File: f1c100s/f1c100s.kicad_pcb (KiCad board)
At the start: 2 copper layers, 47.6 x 52.6 mm, 74 parts, among them IC1 F1C100S, IC2 MCP1703T-2802E_CB, IC3 MCP1703T-2802E_CB, IC4 MCP1703T-2802E_CB, IC5 MCP1703T-2802E_CB, IC6 S25FL256SAGNFI001, J1 USB_B_Micro, J2 Conn_02x18_Odd_Even, J3 Conn_01x06, J4 Conn_02x02_Odd_Even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

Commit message: Work in progress...
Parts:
- added REF**: MountingHole_2.2mm_M2, MountingHole:MountingHole_2.2mm_M2, F.Cu at (190.9, 97.6)
- added REF**: MountingHole_2.2mm_M2, MountingHole:MountingHole_2.2mm_M2, F.Cu at (149.4, 97.7)
- added REF**: MountingHole_2.2mm_M2, MountingHole:MountingHole_2.2mm_M2, F.Cu at (149.4, 52.9)
- added REF**: MountingHole_2.2mm_M2, MountingHole:MountingHole_2.2mm_M2, F.Cu at (190.9, 52.9)
- moved D1 9.40 mm to (160.0, 96.0)
- moved R10 9.40 mm to (163.5, 99.9)
- moved R8 9.40 mm to (163.5, 96.7)
- moved R9 9.40 mm to (163.5, 98.3)
- moved TP1 6.64 mm to (184.4, 99.1)
- moved C18 5.49 mm to (166.5, 52.4)
- moved C19 5.49 mm to (170.1, 54.3)
- moved C21 5.49 mm to (170.7, 55.9)
- moved C23 5.49 mm to (171.3, 54.3)
- moved C35 5.49 mm to (174.7, 52.7)
- moved C36 5.49 mm to (178.8, 52.7)
- moved C37 5.49 mm to (183.2, 52.7)
- moved R3 5.49 mm to (174.7, 54.8)
- moved C17 5.49 mm to (174.7, 53.7)
- moved R4 5.49 mm to (166.5, 53.4)
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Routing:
- net +3V3: track 102.7 -> 235.1 mm, vias 6 -> 16
- net +5V: track 61.0 -> 147.4 mm, vias 1 -> 4
- net GND: track 0.00 -> 72.0 mm, vias 0 -> 16
- net LCD_D20: track 0.00 -> 59.9 mm, vias 0 -> 2
- net LCD_D19: track 0.00 -> 57.9 mm, vias 0 -> 2
- net LCD_D18: track 0.00 -> 49.6 mm, vias 0 -> 2
- net +1V2: track 19.8 -> 66.9 mm, vias 1 -> 4
- net +2V8: track 32.6 -> 78.5 mm, vias 3 -> 5
- net LCD_D15: track 0.00 -> 44.7 mm, vias 0 -> 1
- net LCD_D3: track 0.00 -> 43.3 mm, vias 0 -> 1
- net SPI0_CLK: track 46.3 -> 3.19 mm, vias 3 -> 1
- net LCD_D14: track 0.00 -> 43.1 mm, vias 0 -> 1
- net LCD_D13: track 0.00 -> 41.7 mm, vias 0 -> 1
- net LCD_D4: track 0.00 -> 41.6 mm, vias 0 -> 1
- net LCD_D12: track 0.00 -> 41.4 mm, vias 0 -> 1
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- added copper zone on In2.Cu, net GND
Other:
- board size 47.6 x 52.6 mm -> 47.6 x 57.7 mm
- copper layers 2 -> 4
- net class Default: clearance 0.2 -> 0.09
- rule trace_clearance: 0.2 -> 0.09
- rule trace_min: 0.127 -> 0.09
- rule via_min_drill: 0.3 -> 0.2
- rule via_min_size: 0.6 -> 0.45

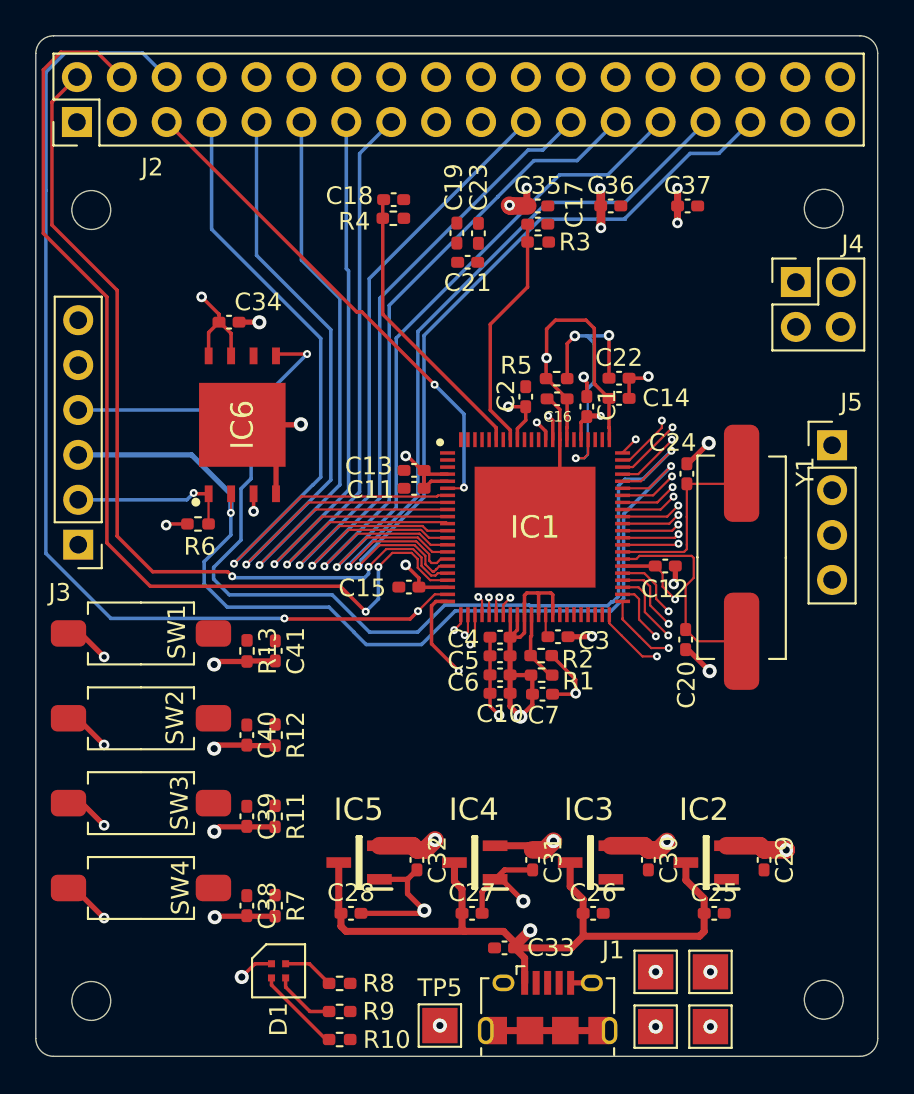
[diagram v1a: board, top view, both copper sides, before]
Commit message: Sadly I have to use a little bit more of GND
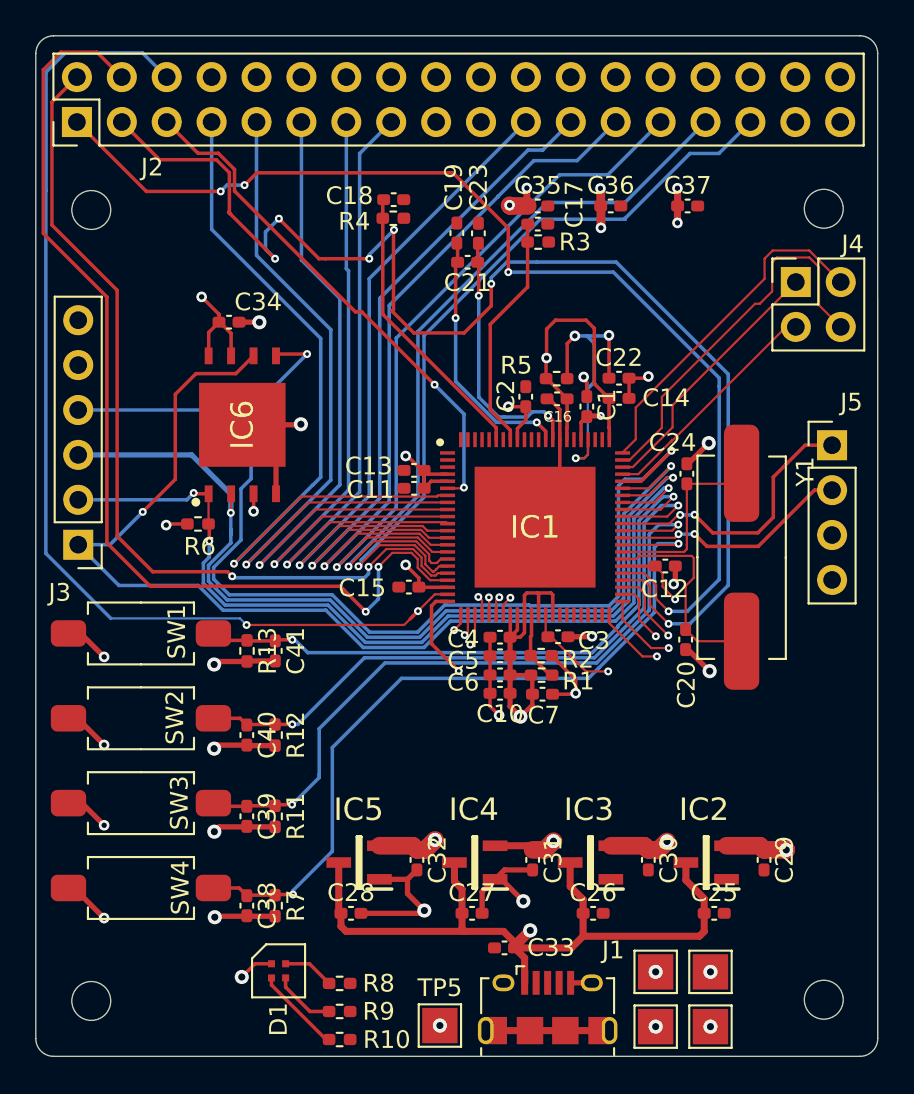
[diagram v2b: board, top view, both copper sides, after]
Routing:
- net LCD_D1: track 4.25 -> 74.3 mm, vias 1 -> 6
- net LCD_D0: track 3.96 -> 63.6 mm, vias 1 -> 4
- net SPI0_CLK: track 3.19 -> 62.5 mm, vias 1 -> 2
- net DEBUG_SW4: track 3.19 -> 43.7 mm, vias 1 -> 2
- net SPI0_CS: track 12.5 -> 50.7 mm, vias 2 -> 3
- net DEBUG_SW3: track 3.30 -> 40.4 mm, vias 1 -> 2
- net DEBUG_SW2: track 3.41 -> 37.8 mm, vias 1 -> 2
- net DEBUG_SW1: track 3.18 -> 36.2 mm, vias 1 -> 2
- net TPX2: track 3.39 -> 22.0 mm, vias 1 -> 0
- net TPX1: track 1.08 -> 19.6 mm, vias 1 -> 0
- net /MPU/TV_VRP: track 1.19 -> 14.6 mm, vias 1 -> 2
- net /MPU/TV_VRN: track 1.46 -> 14.8 mm, vias 1 -> 2
- net UART0_RX: track 3.36 -> 15.9 mm, vias 1 -> 2
- net TPY1: track 3.76 -> 14.9 mm, vias 1 -> 0
- net UART0_TX: track 3.25 -> 13.5 mm, vias 1 -> 2
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
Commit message: Almost ready
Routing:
- net LCD_D21: track 1.03 -> 65.1 mm
- net LCD_D22: track 1.23 -> 64.5 mm
- net LCD_D23: track 1.80 -> 63.9 mm
- net LCD_D16: track 4.30 -> 51.2 mm
- net LCD_D8: track 4.33 -> 51.2 mm, vias 1 -> 4
- net LCD_D17: track 4.33 -> 50.0 mm
- net LCD_DE: track 0.98 -> 45.9 mm, vias 1 -> 2
- net LCD_VSYNC: track 1.12 -> 44.7 mm, vias 1 -> 3
- net DEBUG_LED3: track 0.00 -> 43.2 mm, vias 0 -> 2
- net LCD_HSYNC: track 1.06 -> 43.8 mm, vias 1 -> 3
- net DEBUG_LED2: track 0.00 -> 40.6 mm, vias 0 -> 2
- net LCD_CLK: track 1.09 -> 41.2 mm, vias 1 -> 5
- net LCD_D9: track 3.54 -> 43.3 mm, vias 1 -> 2
- net DEBUG_LED1: track 0.00 -> 38.7 mm, vias 0 -> 2
- net DEBUG_SW1: track 36.2 -> 53.1 mm
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
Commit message: All done i guess. DRC a little bit fuzzy but whatever.
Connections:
- net USB_DM renamed USB_N
- net USB_DP renamed USB_P
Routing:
- net GND: track 71.8 -> 113.4 mm, vias 16 -> 36
- net USB_N: track 1.02 -> 36.4 mm, vias 1 -> 2
- net USB_P: track 1.13 -> 35.3 mm, vias 1 -> 2
- net LCD_VSYNC: track 44.7 -> 48.7 mm
- net LCD_HSYNC: track 43.8 -> 47.5 mm
- net LCD_DE: track 45.9 -> 49.2 mm
- net +5V: track 147.4 -> 146.4 mm
- net DEBUG_SW4: track 46.0 -> 46.8 mm

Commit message: Production files generated.
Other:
- board text added: "F1C100s Linux Dev Board"
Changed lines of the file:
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@@
   (general
     (thickness 1.6)
-    (drawings 8)
+    (drawings 9)
     (tracks 1324)
     (zones 0)
@@
       (outputformat 1)
       (mirror false)
-      (drillshape 1)
+      (drillshape 0)
       (scaleselection 1)
-      (outputdirectory ""))
+      (outputdirectory "../Output/"))
   )
   (net 0 "")
@@
     (tags "Integrated Circuit")
     (attr smd)
-    (fp_text reference IC6 (at 0 0 90) (layer F.SilkS)
+    (fp_text reference IC6 (at 1.6502 4.0874 180) (layer F.SilkS)
       (effects (font (size 1.27 1.27) (thickness 0.254)))
     )
@@
     (at 160.01238 95.98914 270)
     (attr smd)
-    (fp_text reference D1 (at 2.7432 0 270) (layer F.SilkS)
+    (fp_text reference D1 (at 2.3749 0.77978) (layer F.SilkS)
       (effects (font (size 1 1) (thickness 0.15)))
     )
@@
   (module f1c100s:LFXTAL036533 (layer F.Cu)
     (at 186.2074 72.5932 90)
-    (fp_text reference Y1 (at 4.85 3.6 90) (layer F.SilkS)
+    (fp_text reference Y1 (at 0.0432 0.1426 90) (layer F.SilkS)
       (effects (font (size 1 1) (thickness 0.15)))
     )
@@
     (tags "capacitor handsolder")
     (attr smd)
-    (fp_text reference C2 (at 0.05588 -1.1176 90) (layer F.SilkS)
+    (fp_text reference C2 (at -0.28984 -0.99508 90) (layer F.SilkS)
       (effects (font (size 1 1) (thickness 0.15)))
     )
@@
     (tags "capacitor handsolder")
     (attr smd)
-    (fp_text reference C24 (at 1.76276 -0.80772 180) (layer F.SilkS)
+    (fp_text reference C24 (at -0.43 1.39 270) (layer F.SilkS)
       (effects (font (size 1 1) (thickness 0.15)))
     )
@@
     (tags "capacitor handsolder")
     (attr smd)
-    (fp_text reference C25 (at 0 -1.16) (layer F.SilkS)
+    (fp_text reference C25 (at 2.62128 -0.54864) (layer F.SilkS)
       (effects (font (size 1 1) (thickness 0.15)))
     )
@@
     (tags "capacitor handsolder")
     (attr smd)
-    (fp_text reference C26 (at 0 -1.16) (layer F.SilkS)
+    (fp_text reference C26 (at 2.429934 -0.27432) (layer F.SilkS)
       (effects (font (size 1 1) (thickness 0.15)))
     )
@@
     (tags "capacitor handsolder")
     (attr smd)
-    (fp_text reference C27 (at 0 -1.16) (layer F.SilkS)
-      (effects (font (size 1 1) (thickness 0.15)))
+    (fp_text reference C27 (at 2.126827 0.32004) (layer F.SilkS)
+      (effects (font (size 0.7 0.7) (thickness 0.15)))
     )
     (fp_text value 1u (at 0 1.16) (layer F.Fab)
@@
     (tags "capacitor handsolder")
     (attr smd)
-    (fp_text reference C28 (at 0 -1.16) (layer F.SilkS)
+    (fp_text reference C28 (at -0.0635 1.4732) (layer F.SilkS)
       (effects (font (size 1 1) (thickness 0.15)))
     )
@@
     (tags "capacitor handsolder")
     (attr smd)
-    (fp_text reference C31 (at 0 -1.16 90) (layer F.SilkS)
+    (fp_text reference C31 (at -1.68148 0.004353 180) (layer F.SilkS)
       (effects (font (size 1 1) (thickness 0.15)))
     )
@@
     (tags "capacitor handsolder")
     (attr smd)
-    (fp_text reference C32 (at 0 -1.16 90) (layer F.SilkS)
+    (fp_text reference C32 (at -1.70434 0.773611 180) (layer F.SilkS)
       (effects (font (size 1 1) (thickness 0.15)))
     )
@@
     (tags "capacitor handsolder")
     (attr smd)
-    (fp_text reference C34 (at 1.651 -1.13792) (layer F.SilkS)
+    (fp_text reference C34 (at 0.43924 -1.19376) (layer F.SilkS)
       (effects (font (size 1 1) (thickness 0.15)))
     )
@@
     (tags "capacitor handsolder")
     (attr smd)
-    (fp_text reference C35 (at 0 -1.16) (layer F.SilkS)
+    (fp_text reference C35 (at -0.1758 -1.12024) (layer F.SilkS)
       (effects (font (size 1 1) (thickness 0.15)))
     )
@@
     (tags "capacitor handsolder")
     (attr smd)
-    (fp_text reference C38 (at 0 -1.16 90) (layer F.SilkS)
+    (fp_text reference C38 (at 1.72212 0.34036 180) (layer F.SilkS)
       (effects (font (size 1 1) (thickness 0.15)))
     )
@@
     (tags "capacitor handsolder")
     (attr smd)
-    (fp_text reference C39 (at 0 -1.16 90) (layer F.SilkS)
+    (fp_text reference C39 (at 1.79578 -0.08636 180) (layer F.SilkS)
       (effects (font (size 1 1) (thickness 0.15)))
     )
@@
     (tags "capacitor handsolder")
     (attr smd)
-    (fp_text reference C40 (at 0 -1.16 90) (layer F.SilkS)
+    (fp_text reference C40 (at 1.8484 -0.3834 180) (layer F.SilkS)
       (effects (font (size 1 1) (thickness 0.15)))
     )
@@
     (tags "capacitor handsolder")
     (attr smd)
-    (fp_text reference C41 (at 0 -1.16 90) (layer F.SilkS)
+    (fp_text reference C41 (at 1.80836 1.22696 180) (layer F.SilkS)
       (effects (font (size 1 1) (thickness 0.15)))
     )
@@
     (tags "resistor handsolder")
     (attr smd)
-    (fp_text reference R5 (at -2.286 -0.75184) (layer F.SilkS)
+    (fp_text reference R5 (at -2.2926 -0.88908) (layer F.SilkS)
       (effects (font (size 1 1) (thickness 0.15)))
     )
@@
     (tags "resistor handsolder")
     (attr smd)
-    (fp_text reference R6 (at 0.1016 1.27508) (layer F.SilkS)
+    (fp_text reference R6 (at -0.65308 1.24148) (layer F.SilkS)
       (effects (font (size 1 1) (thickness 0.15)))
     )
@@
     (tags "resistor handsolder")
     (attr smd)
-    (fp_text reference R11 (at 0 -1.17 90) (layer F.SilkS)
+    (fp_text reference R11 (at -0.21844 -1.04394 90) (layer F.SilkS)
       (effects (font (size 1 1) (thickness 0.15)))
     )
@@
     (tags "resistor handsolder")
     (attr smd)
-    (fp_text reference R13 (at 0 -1.17 90) (layer F.SilkS)
+    (fp_text reference R13 (at -0.19164 -2.77324 90) (layer F.SilkS)
       (effects (font (size 1 1) (thickness 0.15)))
     )
@@
     )
   )
+  (gr_text "F1C100s Linux Dev Board" (at 174.3456 83.9216) (layer F.SilkS)
+    (effects (font (size 1 1) (thickness 0.15)))
+  )
   (gr_arc (start 192.905059 99.821679) (end 192.905059 100.8253) (angle -90) (layer Edge.Cuts) (width 0.05))

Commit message: Production files ready!
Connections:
- REF** pad 1: (no net) -> GND (x3)
